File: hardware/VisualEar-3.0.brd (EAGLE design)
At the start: 70 x 34 mm, 8 parts

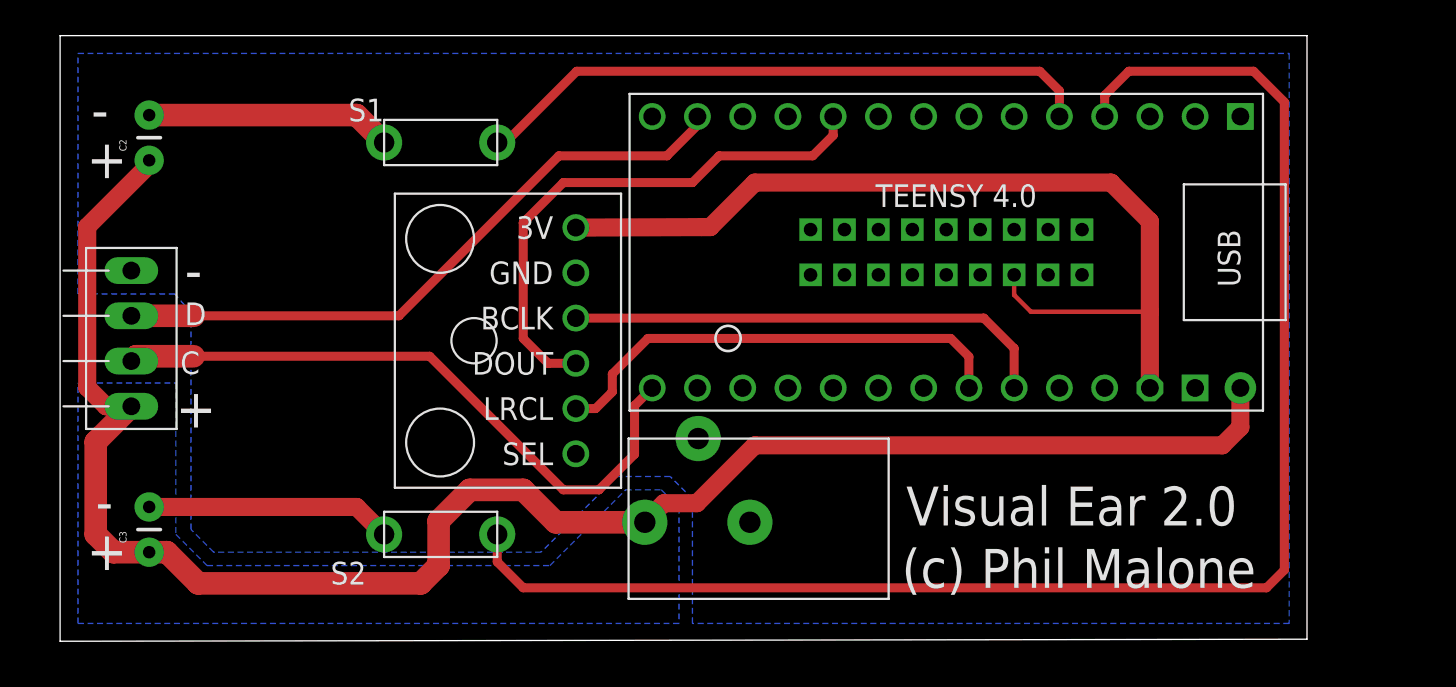
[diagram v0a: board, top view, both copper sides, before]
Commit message: Updated to Single Button 3.0 PCB
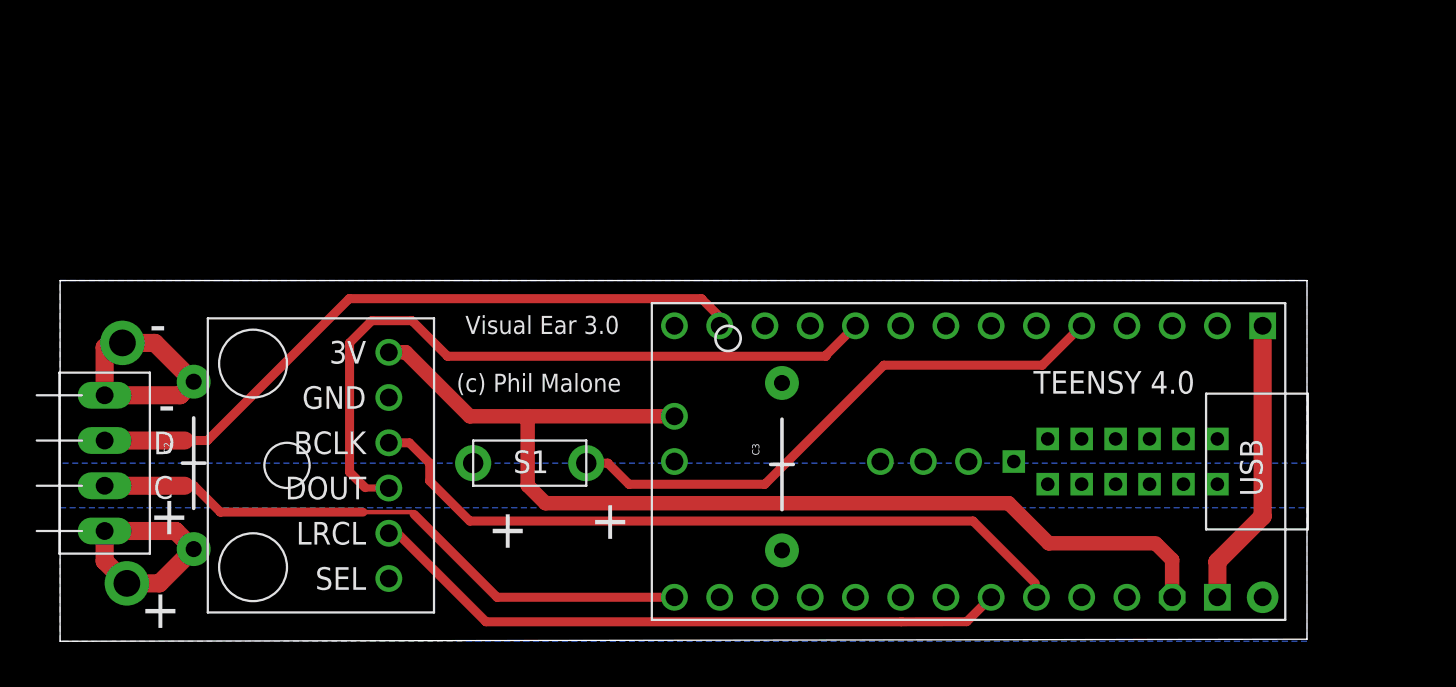
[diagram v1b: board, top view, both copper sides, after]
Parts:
- removed S2: TACTILE-SWITCHTHRU-HOLE, philbot:CLICK-WEL
- removed U$2: 2.1MMJACKTHM, philbot:PJ-102A
- C2, C3: device philbot:CAP-PTH-SMALL -> philbot:CAP-PTH-LARGE
- U$1: value TEENSY40DIP -> TEENSY40DIPPLUS5; device teensy:TEENSY40-DIP -> teensy:TEENSY40-DIP+5
- moved C3 35.9 mm to (40.5, 9.93)
- moved S1 18.7 mm to (27.0, 10.0)
- moved C2 17.2 mm to (7.50, 10.0)
- moved U$3 12.6 mm to (14.6, 9.87)
- moved U$1 11.8 mm to (51.0, 10.1)
- moved U$4 7.16 mm to (2.50, 10.0)
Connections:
- removed net N$1: S2.2, U$1.2-OUT2
- net 5V: no longer U$2.TIP
- net GND: no longer S2.1, U$2.RING, U$2.RING_SW
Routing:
- net 5V: track 99.3 -> 13.4 mm, vias 0 -> 1
- net N$1: track 85.6 -> 0.00 mm
- net 3V: track 52.7 -> 72.9 mm
- net BCLK: track 27.5 -> 41.0 mm
- net DOUT: track 30.5 -> 42.7 mm
- net LRCL: track 26.5 -> 36.4 mm
- net N$2: track 35.1 -> 32.0 mm
- net GND: track 27.7 -> 30.3 mm, vias 0 -> 1
- net DAT: track 36.7 -> 38.8 mm
- net CLK: track 36.4 -> 34.6 mm
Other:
- board size 70 x 34 mm -> 70 x 20.2 mm
- board text added: "Visual Ear 3.0"
- board text removed: "Visual Ear 2.0"
